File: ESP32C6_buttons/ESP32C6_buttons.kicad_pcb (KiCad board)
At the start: 2 copper layers, 33.1 x 30.5 mm, 6 parts, among them J1 Power, SW1 SW_Push, SW2 SW_Push, SW3 SW_Push, SW4 SW_Push, U1 XIAO-ESP32-C6-DIP

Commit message: add buttons
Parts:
- moved J1 2.75 mm to (183.9, 88.0), turned to 90 degrees
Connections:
- J1 pad 1: +3V3 -> GND
- J1 pad 2: GND -> +3V3
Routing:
- net +3V3: track 20.7 -> 19.7 mm
- net GND: track 77.7 -> 77.1 mm
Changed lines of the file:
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@@
 	(footprint "Connector_JST:JST_XH_B2B-XH-A_1x02_P2.50mm_Vertical"
 		(layer "F.Cu")
-		(at 184.9 85.5 -90)
+		(at 183.875 88.05 90)
 		(descr "JST XH series connector, B2B-XH-A (http://www.jst-mfg.com/product/pdf/eng/eXH.pdf), generated with kicad-footprint-generator")
 		(tags "connector JST XH vertical")
@@
 		(attr through_hole)
 		(fp_line
+			(start -1.6 -2.75)
+			(end -2.85 -2.75)
+			(stroke
+				(width 0.12)
+				(type solid)
+			)
+			(layer "F.SilkS")
+		)
+		(fp_line
+			(start -2.85 -2.75)
+			(end -2.85 -1.5)
+			(stroke
+				(width 0.12)
+				(type solid)
+			)
+			(layer "F.SilkS")
+		)
+		(fp_line
+			(start 5.05 -0.2)
+			(end 4.3 -0.2)
+			(stroke
+				(width 0.12)
+				(type solid)
+			)
+			(layer "F.SilkS")
+		)
+		(fp_line
+			(start 4.3 -0.2)
+			(end 4.3 2.75)
+			(stroke
+				(width 0.12)
+				(type solid)
+			)
+			(layer "F.SilkS")
+		)
+		(fp_line
+			(start -1.8 -0.2)
+			(end -1.8 2.75)
+			(stroke
+				(width 0.12)
+				(type solid)
+			)
+			(layer "F.SilkS")
+		)
+		(fp_line
+			(start -2.55 -0.2)
+			(end -1.8 -0.2)
+			(stroke
+				(width 0.12)
+				(type solid)
+			)
+			(layer "F.SilkS")
+		)
+		(fp_line
+			(start 4.3 2.75)
+			(end 1.25 2.75)
+			(stroke
+				(width 0.12)
+				(type solid)
+			)
+			(layer "F.SilkS")
+		)
+		(fp_line
 			(start -1.8 2.75)
 			(end 1.25 2.75)
@@
 			(layer "F.SilkS")
 		)
-		(fp_line
-			(start 4.3 2.75)
-			(end 1.25 2.75)
-			(stroke
-				(width 0.12)
-				(type solid)
-			)
-			(layer "F.SilkS")
-		)
-		(fp_line
-			(start -2.55 -0.2)
-			(end -1.8 -0.2)
-			(stroke
-				(width 0.12)
-				(type solid)
-			)
-			(layer "F.SilkS")
-		)
-		(fp_line
-			(start -1.8 -0.2)
-			(end -1.8 2.75)
-			(stroke
-				(width 0.12)
-				(type solid)
-			)
-			(layer "F.SilkS")
-		)
-		(fp_line
-			(start 4.3 -0.2)
-			(end 4.3 2.75)
-			(stroke
-				(width 0.12)
-				(type solid)
-			)
-			(layer "F.SilkS")
-		)
-		(fp_line
-			(start 5.05 -0.2)
-			(end 4.3 -0.2)
-			(stroke
-				(width 0.12)
-				(type solid)
-			)
-			(layer "F.SilkS")
-		)
-		(fp_line
-			(start -2.85 -2.75)
-			(end -2.85 -1.5)
-			(stroke
-				(width 0.12)
-				(type solid)
-			)
-			(layer "F.SilkS")
-		)
-		(fp_line
-			(start -1.6 -2.75)
-			(end -2.85 -2.75)
-			(stroke
-				(width 0.12)
-				(type solid)
-			)
+		(fp_rect
+			(start -2.56 -2.46)
+			(end 5.06 3.51)
+			(stroke
+				(width 0.12)
+				(type solid)
+			)
+			(fill no)
+			(layer "F.SilkS")
+		)
+		(fp_rect
+			(start 3.25 -2.45)
+			(end 5.05 -1.7)
+			(stroke
+				(width 0.12)
+				(type solid)
+			)
+			(fill no)
+			(layer "F.SilkS")
+		)
+		(fp_rect
+			(start 0.75 -2.45)
+			(end 1.75 -1.7)
+			(stroke
+				(width 0.12)
+				(type solid)
+			)
+			(fill no)
 			(layer "F.SilkS")
 		)
@@
 		)
 		(fp_rect
-			(start 0.75 -2.45)
-			(end 1.75 -1.7)
-			(stroke
-				(width 0.12)
-				(type solid)
-			)
-			(fill no)
-			(layer "F.SilkS")
-		)
-		(fp_rect
-			(start 3.25 -2.45)
-			(end 5.05 -1.7)
-			(stroke
-				(width 0.12)
-				(type solid)
-			)
-			(fill no)
-			(layer "F.SilkS")
-		)
-		(fp_rect
-			(start -2.56 -2.46)
-			(end 5.06 3.51)
-			(stroke
-				(width 0.12)
-				(type solid)
-			)
-			(fill no)
-			(layer "F.SilkS")
-		)
-		(fp_rect
 			(start -2.95 -2.85)
 			(end 5.45 3.9)
@@
 		)
 		(fp_line
+			(start -0.625 -2.35)
+			(end 0 -1.35)
+			(stroke
+				(width 0.1)
+				(type solid)
+			)
+			(layer "F.Fab")
+		)
+		(fp_line
 			(start 0 -1.35)
 			(end 0.625 -2.35)
-			(stroke
-				(width 0.1)
-				(type solid)
-			)
-			(layer "F.Fab")
-		)
-		(fp_line
-			(start -0.625 -2.35)
-			(end 0 -1.35)
 			(stroke
 				(width 0.1)
@@
 		)
 		(pad "1" thru_hole roundrect
-			(at 0 0 270)
+			(at 0 0 90)
 			(size 1.7 2)
 			(drill 1)
@@
 			(remove_unused_layers no)
 			(roundrect_rratio 0.147059)
-			(net 2 "+3V3")
+			(net 1 "GND")
 			(pinfunction "Pin_1")
 			(pintype "passive")
 		)
 		(pad "2" thru_hole oval
-			(at 2.5 0 270)
+			(at 2.5 0 90)
 			(size 1.7 2)
 			(drill 1)
 			(layers "*.Cu" "*.Mask")
 			(remove_unused_layers no)
-			(net 1 "GND")
+			(net 2 "+3V3")
 			(pinfunction "Pin_2")
 			(pintype "passive")
@@
 	)
 	(segment
+		(start 187.7 98.7)
+		(end 183.9 94.9)
+		(width 0.5)
+		(layer "B.Cu")
+		(net 1)
+	)
+	(segment
 		(start 173.2 106.3)
 		(end 170.6 103.7)
@@
 	)
 	(segment
-		(start 184.9 88)
-		(end 167.1265 88)
-		(width 0.5)
-		(layer "B.Cu")
-		(net 1)
-	)
-	(segment
 		(start 168 106.3)
 		(end 160.2 106.3)
@@
 	)
 	(segment
-		(start 187.7 98.7)
-		(end 187.7 103.7)
+		(start 183.825 88)
+		(end 167.1265 88)
+		(width 0.5)
+		(layer "B.Cu")
+		(net 1)
+	)
+	(segment
+		(start 183.9 94.9)
+		(end 183.9 88.075)
 		(width 0.5)
 		(layer "B.Cu")
@@
 	)
 	(segment
-		(start 167.1265 88)
-		(end 162.5225 83.396)
-		(width 0.5)
-		(layer "B.Cu")
-		(net 1)
-	)
-	(segment
-		(start 184.9 88)
-		(end 184.9 95.9)
+		(start 183.9 88.075)
+		(end 183.825 88)
 		(width 0.5)
 		(layer "B.Cu")
@@
 	)
 	(segment
-		(start 184.9 95.9)
+		(start 187.7 103.7)
 		(end 187.7 98.7)
 		(width 0.5)
@@
 	)
 	(segment
+		(start 167.1265 88)
+		(end 162.5225 83.396)
+		(width 0.5)
+		(layer "B.Cu")
+		(net 1)
+	)
+	(segment
 		(start 167.1665 85.5)
-		(end 184.9 85.5)
+		(end 183.825 85.5)
 		(width 0.5)
 		(layer "B.Cu")
@@
 		(width 0.5)
 		(layer "B.Cu")
+		(net 2)
+	)
+	(segment
+		(start 183.825 85.5)
+		(end 183.875 85.55)
+		(width 0.5)
+		(layer "B.Cu")

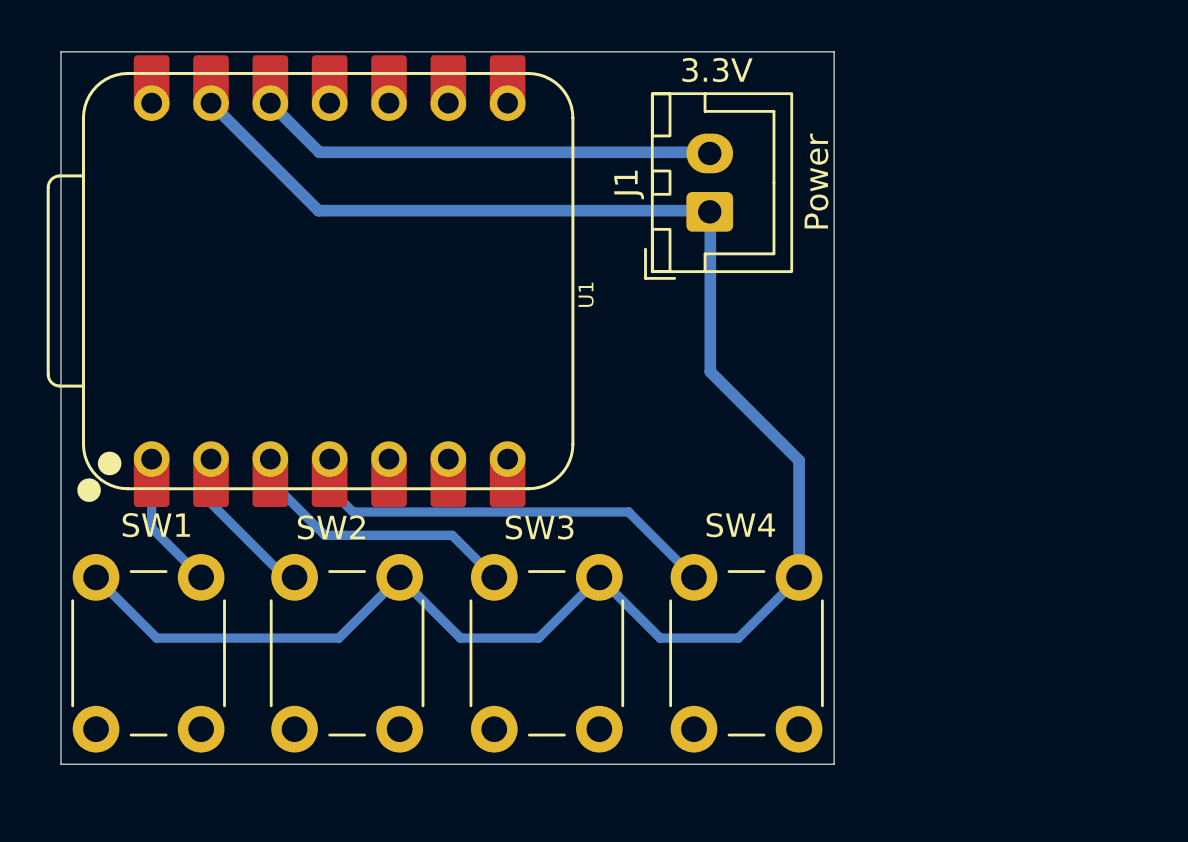
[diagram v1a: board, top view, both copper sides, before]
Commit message: update to add rectifier
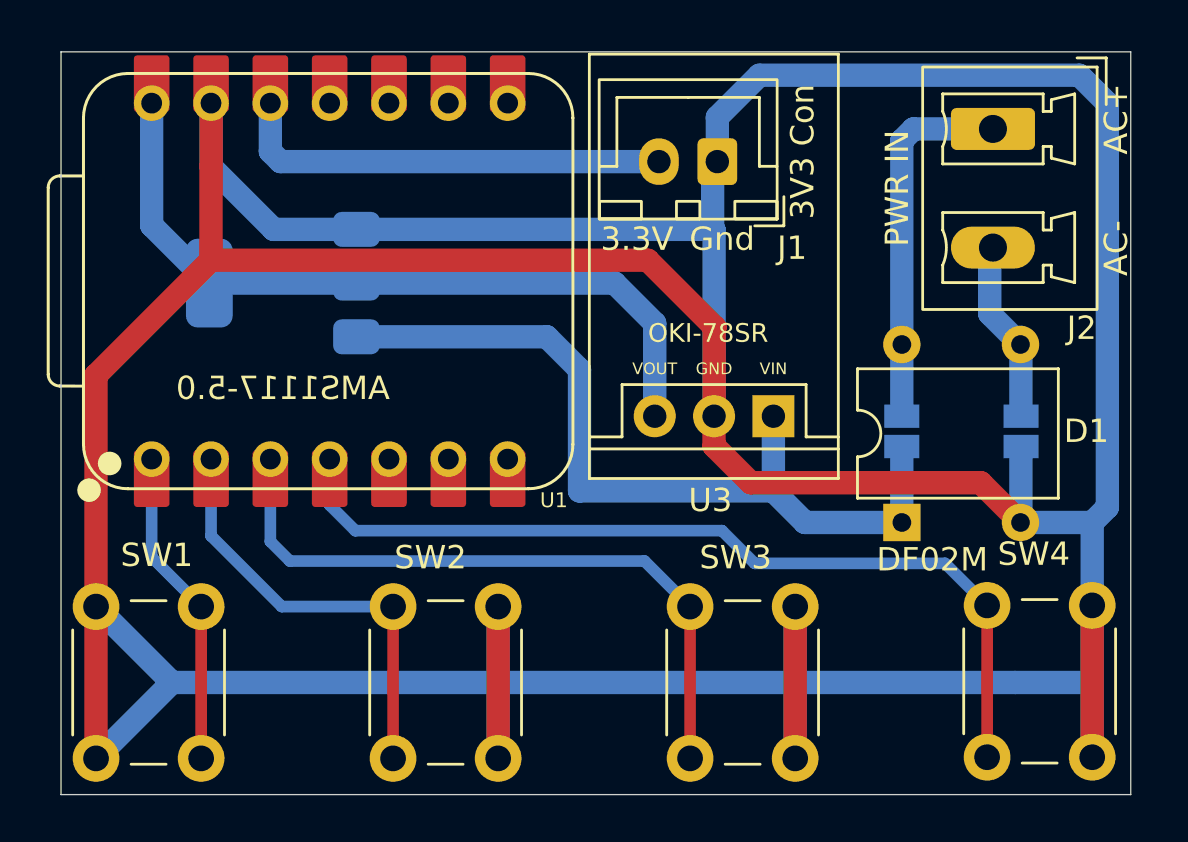
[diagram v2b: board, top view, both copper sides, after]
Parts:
- added D1: DF02M, Diode_THT:Diode_Bridge_DIP-4_W7.62mm_P5.08mm, F.Cu at (192.1, 101.3)
- added J2: PWR IN, Connector_Phoenix_MC_HighVoltage:PhoenixContact_MCV_1,5_2-G-5.08_1x02_P5.08mm_Vertical, F.Cu at (196.0, 84.5)
- added JP1: JMP_12V, Jumper:SolderJumper-2_P1.3mm_Open_Pad1.0x1.5mm, B.Cu at (192.1, 97.4)
- added JP2: JMP_GND, Jumper:SolderJumper-2_P1.3mm_Open_Pad1.0x1.5mm, B.Cu at (197.2, 97.4)
- added U2: AMS1117-5.0, Package_TO_SOT_SMD:SOT-223-3_TabPin2, B.Cu at (165.6, 91.1)
- added U3: L7805, V_REG:OKI-78SR_Horz, F.Cu at (186.6, 96.8)
- J1: value Power -> 3V3 Con
- moved SW4 12.6 mm to (200.2, 104.9)
- moved SW3 8.48 mm to (187.5, 105.0)
- moved SW2 4.40 mm to (174.8, 105.0)
- moved J1 2.17 mm to (184.2, 85.9), turned to 180 degrees
- moved SW1 1.25 mm to (157.6, 111.5)
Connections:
- U1 pad 14: unconnected-(U1-VBUS-Pad14) -> +5V
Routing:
- net GND: track 77.1 -> 243.8 mm
- net +12V: track 0.00 -> 36.0 mm
- net +5V: track 0.00 -> 32.5 mm
- net Net-(U1-GPIO21/D3): track 18.4 -> 38.4 mm
- net Net-(U1-GPIO2/A2/D2): track 12.2 -> 29.2 mm
- net /AC+: track 0.00 -> 15.8 mm
- net Net-(U1-GPIO1/A1/D1): track 6.78 -> 18.8 mm
- net Net-(U1-GPIO0/A0/D0): track 5.94 -> 13.7 mm
- net /AC-: track 0.00 -> 7.65 mm
- net +3V3: track 19.7 -> 18.9 mm
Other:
- board size 33.1 x 30.5 mm -> 45.8 x 31.8 mm
- board text added: "AC+"
- board text added: "AC-"
